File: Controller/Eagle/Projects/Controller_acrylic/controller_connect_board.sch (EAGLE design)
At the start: 10 parts, among them J1 GIMBAL_3PIN, J2 GIMBAL_3PIN, J3 GIMBAL_3PIN, J4 GIMBAL_3PIN

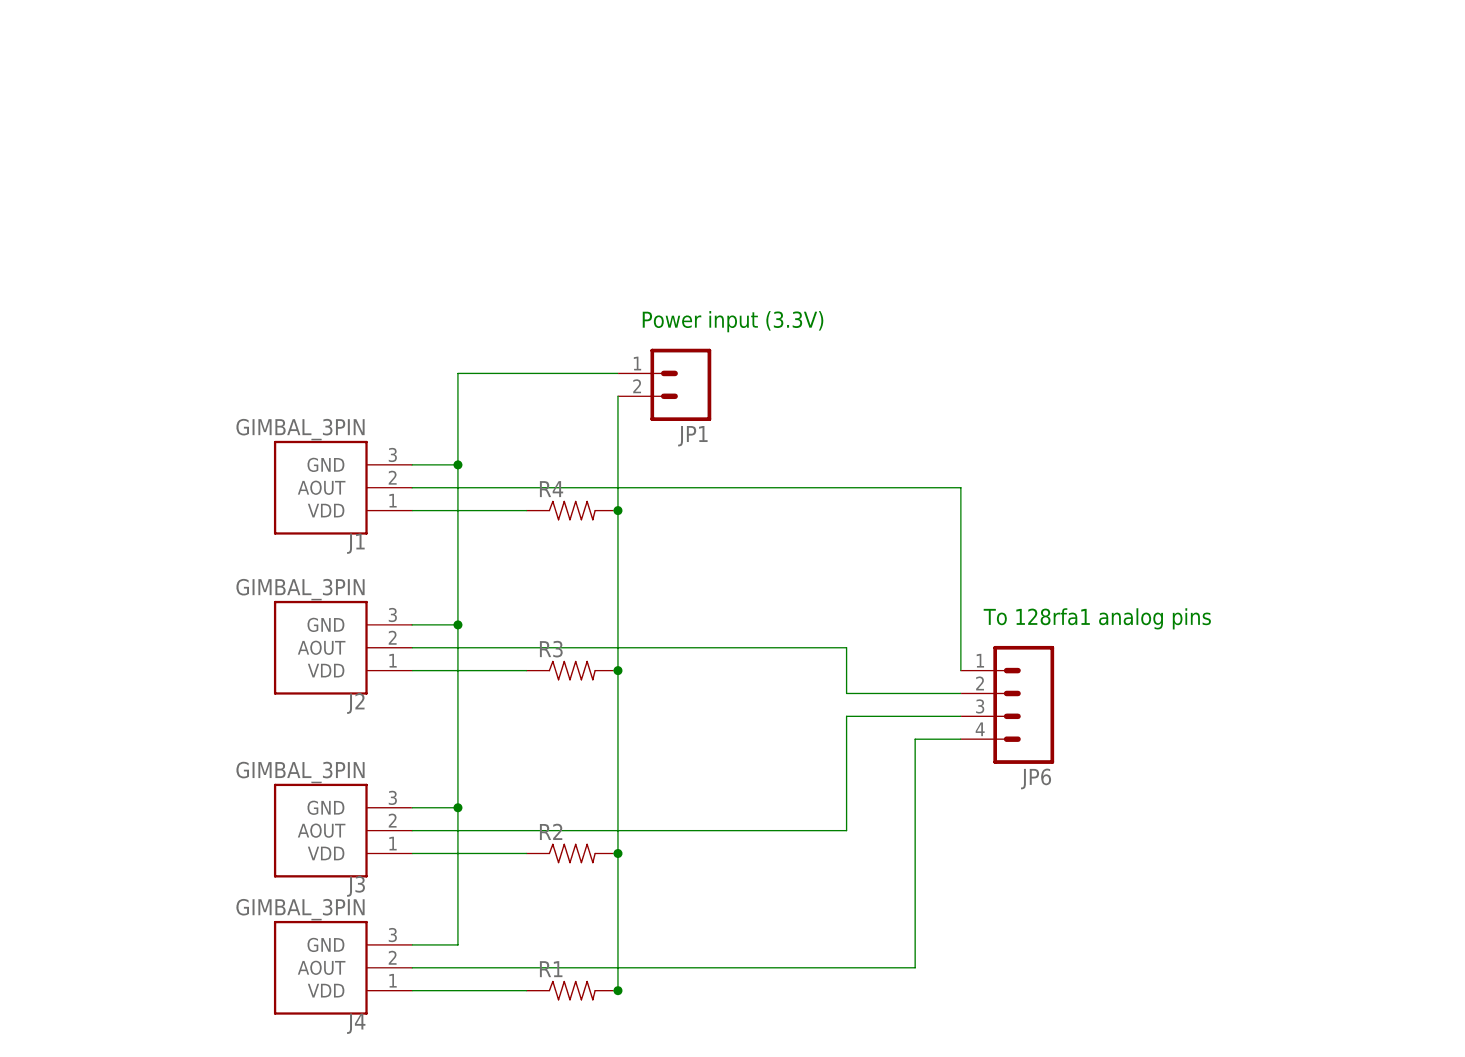
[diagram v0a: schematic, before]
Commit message: Made new eagle project for controller connector board Made new JST connect device that matches the JST connector (not sure why it didn't originally)
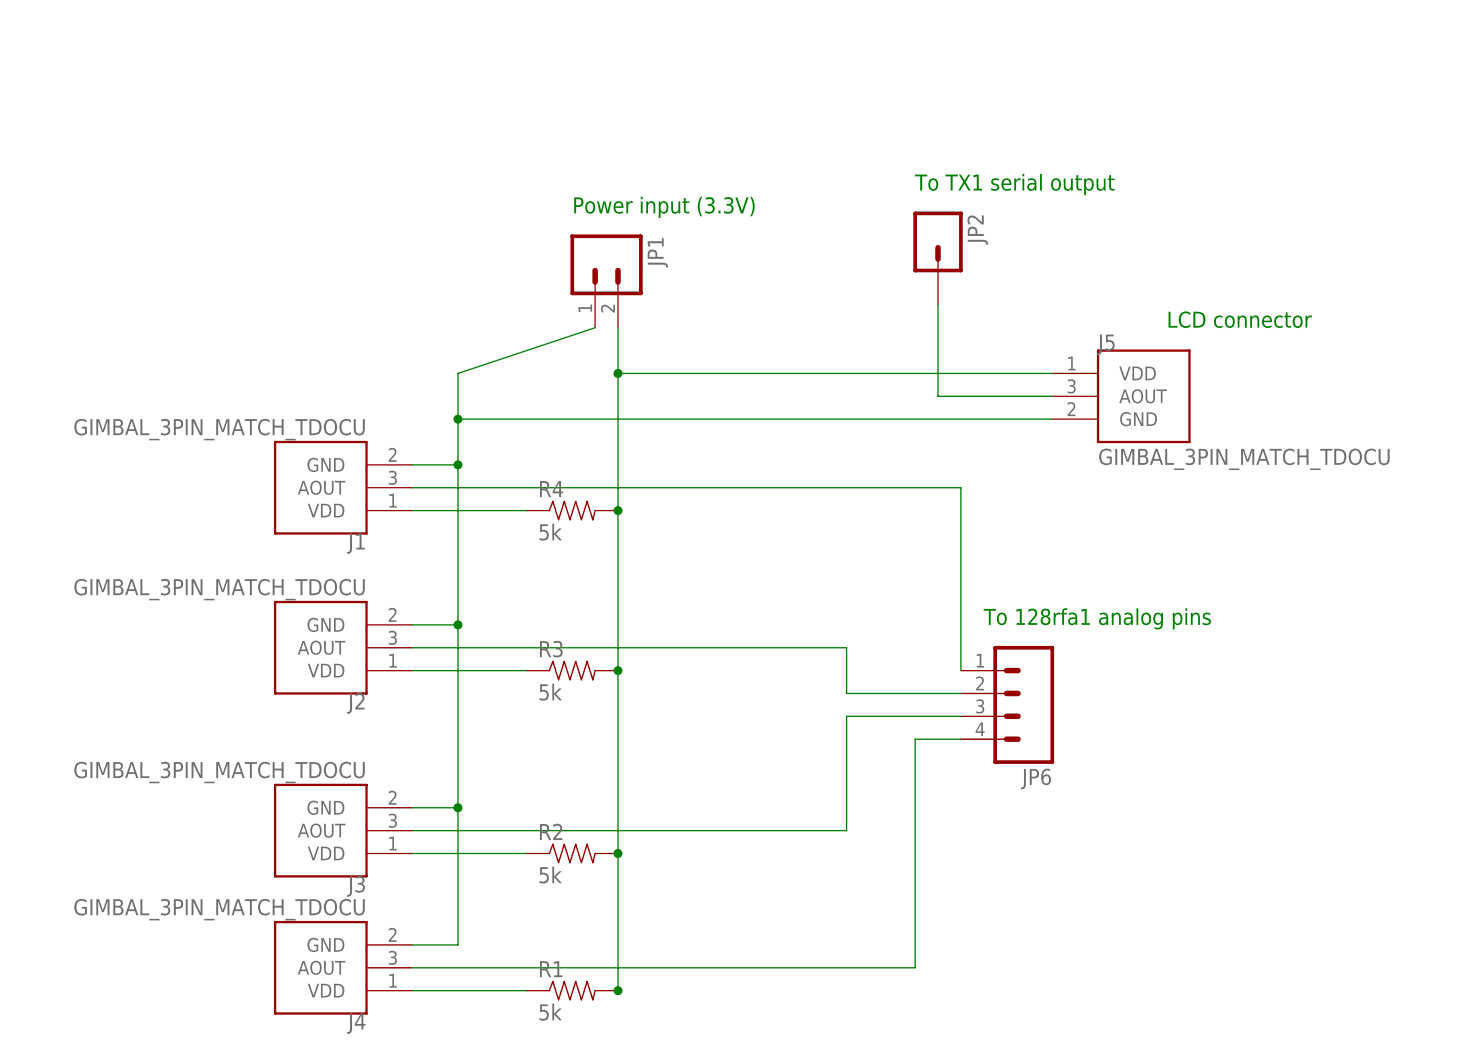
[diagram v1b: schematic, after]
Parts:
- added J5: GIMBAL_3PIN_MATCH_TDOCU, Controller:GIMBAL_3PIN_MATCH_TDOCU
- added JP2: (no value), SparkFun-Connectors:M01PTH
- J1, J2, J3, J4: value GIMBAL_3PIN -> GIMBAL_3PIN_MATCH_TDOCU; device Controller:GIMBAL_3PIN -> Controller:GIMBAL_3PIN_MATCH_TDOCU
- R1, R2, R3, R4: value (none) -> 5k
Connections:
- new net N$9: J5.AOUT, JP2.1
- net 3.3V: now also J5.VDD
- net GND: now also J5.GND
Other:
- note added: "LCD connector"
- note added: "To TX1 serial output"
- moved on the sheet: JP1
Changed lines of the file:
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@@
 </classes>
 <parts>
-<part name="J1" library="Controller" deviceset="GIMBAL_3PIN" device=""/>
-<part name="J2" library="Controller" deviceset="GIMBAL_3PIN" device=""/>
-<part name="J3" library="Controller" deviceset="GIMBAL_3PIN" device=""/>
-<part name="J4" library="Controller" deviceset="GIMBAL_3PIN" device=""/>
-<part name="R1" library="SparkFun-Resistors" deviceset="RESISTOR" device="PTH-1/6W"/>
-<part name="R2" library="SparkFun-Resistors" deviceset="RESISTOR" device="PTH-1/6W"/>
-<part name="R3" library="SparkFun-Resistors" deviceset="RESISTOR" device="PTH-1/6W"/>
-<part name="R4" library="SparkFun-Resistors" deviceset="RESISTOR" device="PTH-1/6W"/>
+<part name="J1" library="Controller" deviceset="GIMBAL_3PIN_MATCH_TDOCU" device=""/>
+<part name="J2" library="Controller" deviceset="GIMBAL_3PIN_MATCH_TDOCU" device=""/>
+<part name="J3" library="Controller" deviceset="GIMBAL_3PIN_MATCH_TDOCU" device=""/>
+<part name="J4" library="Controller" deviceset="GIMBAL_3PIN_MATCH_TDOCU" device=""/>
+<part name="R1" library="SparkFun-Resistors" deviceset="RESISTOR" device="PTH-1/6W" value="5k"/>
+<part name="R2" library="SparkFun-Resistors" deviceset="RESISTOR" device="PTH-1/6W" value="5k"/>
+<part name="R3" library="SparkFun-Resistors" deviceset="RESISTOR" device="PTH-1/6W" value="5k"/>
+<part name="R4" library="SparkFun-Resistors" deviceset="RESISTOR" device="PTH-1/6W" value="5k"/>
 <part name="JP6" library="SparkFun-Connectors" deviceset="M04" device="PTH"/>
 <part name="JP1" library="SparkFun-Connectors" deviceset="M02" device="1X02_NO_SILK"/>
+<part name="J5" library="Controller" deviceset="GIMBAL_3PIN_MATCH_TDOCU" device=""/>
+<part name="JP2" library="SparkFun-Connectors" deviceset="M01" device="PTH"/>
 </parts>
 <sheets>
 <sheet>
 <plain>
-<text x="63.5" y="83.82" size="1.778" layer="91">Power input (3.3V)</text>
+<text x="55.88" y="96.52" size="1.778" layer="91">Power input (3.3V)</text>
 <text x="101.6" y="50.8" size="1.778" layer="91">To 128rfa1 analog pins</text>
+<text x="121.92" y="83.82" size="1.778" layer="91">LCD connector</text>
+<text x="93.98" y="99.06" size="1.778" layer="91">To TX1 serial output</text>
 </plain>
 <instances>
@@
 <instance part="R4" gate="G$1" x="55.88" y="63.5"/>
 <instance part="JP6" gate="G$1" x="104.14" y="43.18" rot="R180"/>
-<instance part="JP1" gate="G$1" x="68.58" y="78.74" rot="R180"/>
+<instance part="JP1" gate="G$1" x="58.42" y="91.44" rot="R270"/>
+<instance part="J5" gate="G$1" x="114.3" y="71.12"/>
+<instance part="JP2" gate="G$1" x="96.52" y="93.98" rot="R270"/>
 </instances>
 <busses>
@@
 <junction x="43.18" y="30.48"/>
 <junction x="43.18" y="50.8"/>
-<wire x1="43.18" y1="68.58" x2="43.18" y2="78.74" width="0.1524" layer="91"/>
+<wire x1="43.18" y1="68.58" x2="43.18" y2="73.66" width="0.1524" layer="91"/>
 <pinref part="JP1" gate="G$1" pin="1"/>
-<wire x1="43.18" y1="78.74" x2="60.96" y2="78.74" width="0.1524" layer="91"/>
+<wire x1="43.18" y1="73.66" x2="43.18" y2="78.74" width="0.1524" layer="91"/>
+<wire x1="43.18" y1="78.74" x2="58.42" y2="83.82" width="0.1524" layer="91"/>
 <junction x="43.18" y="68.58"/>
+<pinref part="J5" gate="G$1" pin="GND"/>
+<wire x1="109.22" y1="73.66" x2="43.18" y2="73.66" width="0.1524" layer="91"/>
+<junction x="43.18" y="73.66"/>
 </segment>
 </net>
@@
 <junction x="60.96" y="63.5"/>
 <pinref part="JP1" gate="G$1" pin="2"/>
-<wire x1="60.96" y1="76.2" x2="60.96" y2="63.5" width="0.1524" layer="91"/>
+<wire x1="60.96" y1="83.82" x2="60.96" y2="78.74" width="0.1524" layer="91"/>
+<pinref part="J5" gate="G$1" pin="VDD"/>
+<wire x1="60.96" y1="78.74" x2="60.96" y2="63.5" width="0.1524" layer="91"/>
+<wire x1="109.22" y1="78.74" x2="60.96" y2="78.74" width="0.1524" layer="91"/>
+<junction x="60.96" y="78.74"/>
 </segment>
 </net>
@@
 </segment>
 </net>
+<net name="N$9" class="0">
+<segment>
+<pinref part="J5" gate="G$1" pin="AOUT"/>
+<pinref part="JP2" gate="G$1" pin="1"/>
+<wire x1="109.22" y1="76.2" x2="96.52" y2="76.2" width="0.1524" layer="91"/>
+<wire x1="96.52" y1="76.2" x2="96.52" y2="86.36" width="0.1524" layer="91"/>
+</segment>
+</net>

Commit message: First test of connector board Ground and VDD were reversed on gimbal pins Made holes bigger
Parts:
- J1, J2, J3, J4: value GIMBAL_3PIN_MATCH_TDOCU -> JST_3PIN_GND_VDD_SIG; device Controller:GIMBAL_3PIN_MATCH_TDOCU -> Controller:JST_3PIN_GND_VDD_SIG
- R1, R2, R3, R4: device SparkFun-Resistors:RESISTORPTH-1/6W -> SparkFun-Resistors:RESISTORPTH-1/4W
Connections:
- net N$5 renamed PITCH
- net N$6 renamed ROLL
- net N$7 renamed THROTTLE
- net N$8 renamed YAW
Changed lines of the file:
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@@
 <layer number="160" name="tMountFaceplate" color="11" fill="1" visible="no" active="yes"/>
 <layer number="161" name="bMountFaceplate" color="11" fill="1" visible="no" active="yes"/>
+<layer number="162" name="tCopperArt" color="7" fill="1" visible="yes" active="yes"/>
+<layer number="163" name="bCopperArt" color="7" fill="1" visible="yes" active="yes"/>
+<layer number="164" name="tRubout" color="13" fill="11" visible="yes" active="yes"/>
+<layer number="165" name="bRubout" color="3" fill="5" visible="yes" active="yes"/>
+<layer number="167" name="Fiducials" color="7" fill="1" visible="yes" active="yes"/>
 <layer number="199" name="Contour" color="7" fill="1" visible="yes" active="yes"/>
 <layer number="200" name="200bmp" color="7" fill="1" visible="yes" active="yes"/>
@@
 <layer number="230" name="230bmp" color="7" fill="1" visible="yes" active="yes"/>
 <layer number="231" name="231bmp" color="7" fill="1" visible="yes" active="yes"/>
+<layer number="232" name="Eagle3D_PG2" color="7" fill="1" visible="no" active="no"/>
+<layer number="233" name="Eagle3D_PG3" color="7" fill="1" visible="no" active="no"/>
 <layer number="248" name="Housing" color="7" fill="1" visible="yes" active="yes"/>
 <layer number="249" name="Edge" color="7" fill="1" visible="yes" active="yes"/>
@@
 </classes>
 <parts>
-<part name="J1" library="Controller" deviceset="GIMBAL_3PIN_MATCH_TDOCU" device=""/>
-<part name="J2" library="Controller" deviceset="GIMBAL_3PIN_MATCH_TDOCU" device=""/>
-<part name="J3" library="Controller" deviceset="GIMBAL_3PIN_MATCH_TDOCU" device=""/>
-<part name="J4" library="Controller" deviceset="GIMBAL_3PIN_MATCH_TDOCU" device=""/>
-<part name="R1" library="SparkFun-Resistors" deviceset="RESISTOR" device="PTH-1/6W" value="5k"/>
-<part name="R2" library="SparkFun-Resistors" deviceset="RESISTOR" device="PTH-1/6W" value="5k"/>
-<part name="R3" library="SparkFun-Resistors" deviceset="RESISTOR" device="PTH-1/6W" value="5k"/>
-<part name="R4" library="SparkFun-Resistors" deviceset="RESISTOR" device="PTH-1/6W" value="5k"/>
+<part name="J1" library="Controller" deviceset="JST_3PIN_GND_VDD_SIG" device=""/>
+<part name="J2" library="Controller" deviceset="JST_3PIN_GND_VDD_SIG" device=""/>
+<part name="J3" library="Controller" deviceset="JST_3PIN_GND_VDD_SIG" device=""/>
+<part name="J4" library="Controller" deviceset="JST_3PIN_GND_VDD_SIG" device=""/>
+<part name="R1" library="SparkFun-Resistors" deviceset="RESISTOR" device="PTH-1/4W" value="5k"/>
+<part name="R2" library="SparkFun-Resistors" deviceset="RESISTOR" device="PTH-1/4W" value="5k"/>
+<part name="R3" library="SparkFun-Resistors" deviceset="RESISTOR" device="PTH-1/4W" value="5k"/>
+<part name="R4" library="SparkFun-Resistors" deviceset="RESISTOR" device="PTH-1/4W" value="5k"/>
 <part name="JP6" library="SparkFun-Connectors" deviceset="M04" device="PTH"/>
 <part name="JP1" library="SparkFun-Connectors" deviceset="M02" device="1X02_NO_SILK"/>
@@
 </segment>
 </net>
-<net name="N$5" class="0">
+<net name="PITCH" class="0">
 <segment>
 <pinref part="J1" gate="G$1" pin="AOUT"/>
@@
 <pinref part="JP6" gate="G$1" pin="1"/>
 <wire x1="99.06" y1="66.04" x2="99.06" y2="45.72" width="0.1524" layer="91"/>
-</segment>
-</net>
-<net name="N$6" class="0">
+<label x="71.12" y="66.04" size="1.778" layer="95"/>
+</segment>
+</net>
+<net name="ROLL" class="0">
 <segment>
 <pinref part="J2" gate="G$1" pin="AOUT"/>
@@
 <pinref part="JP6" gate="G$1" pin="2"/>
 <wire x1="86.36" y1="43.18" x2="99.06" y2="43.18" width="0.1524" layer="91"/>
-</segment>
-</net>
-<net name="N$7" class="0">
+<label x="71.12" y="48.26" size="1.778" layer="95"/>
+</segment>
+</net>
+<net name="THROTTLE" class="0">
 <segment>
 <pinref part="J3" gate="G$1" pin="AOUT"/>
@@
 <pinref part="JP6" gate="G$1" pin="3"/>
 <wire x1="86.36" y1="40.64" x2="99.06" y2="40.64" width="0.1524" layer="91"/>
-</segment>
-</net>
-<net name="N$8" class="0">
+<label x="68.58" y="27.94" size="1.778" layer="95"/>
+</segment>
+</net>
+<net name="YAW" class="0">
 <segment>
 <pinref part="J4" gate="G$1" pin="AOUT"/>
@@
 <pinref part="JP6" gate="G$1" pin="4"/>
 <wire x1="93.98" y1="38.1" x2="99.06" y2="38.1" width="0.1524" layer="91"/>
-</segment>
-</net>
+<label x="71.12" y="12.7" size="1.778" layer="95"/>
+</segment>
+</net>

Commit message: FORGOT THE BUTTON WOW WOW I...WOW
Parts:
- added BUTTON: (no value), SparkFun-Connectors:M01PTH
- added R5: ~10k, SparkFun-Resistors:RESISTORPTH-1/4W
- added U$2: BUTTON-TACTILE-SQUARE, Controller:BUTTON-TACTILE-SQUARE
- R1, R2, R3, R4: value 5k -> 5k-8.2k
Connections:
- new net N$6: BUTTON.1, R5.2, U$2.S, U$2.S1
- net 3.3V: now also U$2.P, U$2.P1
- net GND: now also R5.1
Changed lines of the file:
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@@
 <part name="J3" library="Controller" deviceset="JST_3PIN_GND_VDD_SIG" device=""/>
 <part name="J4" library="Controller" deviceset="JST_3PIN_GND_VDD_SIG" device=""/>
-<part name="R1" library="SparkFun-Resistors" deviceset="RESISTOR" device="PTH-1/4W" value="5k"/>
-<part name="R2" library="SparkFun-Resistors" deviceset="RESISTOR" device="PTH-1/4W" value="5k"/>
-<part name="R3" library="SparkFun-Resistors" deviceset="RESISTOR" device="PTH-1/4W" value="5k"/>
-<part name="R4" library="SparkFun-Resistors" deviceset="RESISTOR" device="PTH-1/4W" value="5k"/>
+<part name="R1" library="SparkFun-Resistors" deviceset="RESISTOR" device="PTH-1/4W" value="5k-8.2k"/>
+<part name="R2" library="SparkFun-Resistors" deviceset="RESISTOR" device="PTH-1/4W" value="5k-8.2k"/>
+<part name="R3" library="SparkFun-Resistors" deviceset="RESISTOR" device="PTH-1/4W" value="5k-8.2k"/>
+<part name="R4" library="SparkFun-Resistors" deviceset="RESISTOR" device="PTH-1/4W" value="5k-8.2k"/>
 <part name="JP6" library="SparkFun-Connectors" deviceset="M04" device="PTH"/>
 <part name="JP1" library="SparkFun-Connectors" deviceset="M02" device="1X02_NO_SILK"/>
 <part name="J5" library="Controller" deviceset="GIMBAL_3PIN_MATCH_TDOCU" device=""/>
 <part name="JP2" library="SparkFun-Connectors" deviceset="M01" device="PTH"/>
+<part name="U$2" library="Controller" deviceset="BUTTON-TACTILE" device="-SQUARE"/>
+<part name="BUTTON" library="SparkFun-Connectors" deviceset="M01" device="PTH"/>
+<part name="R5" library="SparkFun-Resistors" deviceset="RESISTOR" device="PTH-1/4W" value="~10k"/>
 </parts>
 <sheets>
@@
 <instance part="J5" gate="G$1" x="114.3" y="71.12"/>
 <instance part="JP2" gate="G$1" x="96.52" y="93.98" rot="R270"/>
+<instance part="U$2" gate="G$1" x="86.36" y="109.22" rot="R270"/>
+<instance part="BUTTON" gate="G$1" x="129.54" y="111.76" rot="R270"/>
+<instance part="R5" gate="G$1" x="88.9" y="93.98" rot="R90"/>
 </instances>
 <busses>
@@
 <junction x="43.18" y="68.58"/>
 <pinref part="J5" gate="G$1" pin="GND"/>
-<wire x1="109.22" y1="73.66" x2="43.18" y2="73.66" width="0.1524" layer="91"/>
+<wire x1="109.22" y1="73.66" x2="88.9" y2="73.66" width="0.1524" layer="91"/>
 <junction x="43.18" y="73.66"/>
+<label x="73.66" y="73.66" size="1.778" layer="95" rot="R180"/>
+<pinref part="R5" gate="G$1" pin="1"/>
+<wire x1="88.9" y1="73.66" x2="43.18" y2="73.66" width="0.1524" layer="91"/>
+<wire x1="88.9" y1="88.9" x2="88.9" y2="73.66" width="0.1524" layer="91"/>
+<junction x="88.9" y="73.66"/>
 </segment>
 </net>
@@
 <pinref part="J5" gate="G$1" pin="VDD"/>
 <wire x1="60.96" y1="78.74" x2="60.96" y2="63.5" width="0.1524" layer="91"/>
-<wire x1="109.22" y1="78.74" x2="60.96" y2="78.74" width="0.1524" layer="91"/>
+<wire x1="109.22" y1="78.74" x2="78.74" y2="78.74" width="0.1524" layer="91"/>
 <junction x="60.96" y="78.74"/>
+<label x="73.66" y="78.74" size="1.778" layer="95" rot="R180"/>
+<pinref part="U$2" gate="G$1" pin="P1"/>
+<wire x1="78.74" y1="78.74" x2="60.96" y2="78.74" width="0.1524" layer="91"/>
+<wire x1="81.28" y1="106.68" x2="78.74" y2="106.68" width="0.1524" layer="91"/>
+<wire x1="78.74" y1="106.68" x2="78.74" y2="78.74" width="0.1524" layer="91"/>
+<junction x="78.74" y="78.74"/>
+<pinref part="U$2" gate="G$1" pin="P"/>
+<wire x1="81.28" y1="109.22" x2="81.28" y2="106.68" width="0.1524" layer="91"/>
 </segment>
 </net>
@@
 </segment>
 </net>
+<net name="N$6" class="0">
+<segment>
+<pinref part="U$2" gate="G$1" pin="S1"/>
+<wire x1="91.44" y1="106.68" x2="121.92" y2="106.68" width="0.1524" layer="91"/>
+<wire x1="121.92" y1="106.68" x2="121.92" y2="104.14" width="0.1524" layer="91"/>
+<pinref part="BUTTON" gate="G$1" pin="1"/>
+<wire x1="121.92" y1="104.14" x2="129.54" y2="104.14" width="0.1524" layer="91"/>
+<wire x1="91.44" y1="106.68" x2="91.44" y2="104.14" width="0.1524" layer="91"/>
+<pinref part="R5" gate="G$1" pin="2"/>
+<wire x1="91.44" y1="104.14" x2="88.9" y2="104.14" width="0.1524" layer="91"/>
+<wire x1="88.9" y1="104.14" x2="88.9" y2="99.06" width="0.1524" layer="91"/>
+<pinref part="U$2" gate="G$1" pin="S"/>
+<wire x1="91.44" y1="109.22" x2="91.44" y2="106.68" width="0.1524" layer="91"/>
+</segment>
+</net>
